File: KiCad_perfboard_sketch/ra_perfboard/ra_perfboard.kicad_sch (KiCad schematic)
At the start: 20 parts, among them J1 M1, J10 L6, J2 M2, J3 Terminal, J4 USART, J5 L3, J6 L1, J7 L2, J8 L4, J9 L5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

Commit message: Removed bug in LUT set speed function. Updates to MATLAB GUI and KiCad perfboard. Successfully tested TCA9548A library.
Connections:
- net M2_DIR: now also U4.7 (PA1); no longer U4.9 (PA3)
- net M2_EN: now also U4.9 (PA3); no longer U4.10 (PA4)
- net M2_STEP: now also U4.8 (PA2); no longer U4.11 (PA5)
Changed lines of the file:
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@@
 	(wire
 		(pts
-			(xy 130.81 66.04) (xy 129.54 66.04)
+			(xy 40.64 120.65) (xy 40.64 121.92)
+		)
+		(stroke
+			(width 0)
+			(type default)
+		)
+	)
+	(wire
+		(pts
+			(xy 158.75 74.93) (xy 160.02 74.93)
+		)
+		(stroke
+			(width 0)
+			(type default)
+		)
+	)
+	(wire
+		(pts
+			(xy 74.93 147.32) (xy 76.2 147.32)
+		)
+		(stroke
+			(width 0)
+			(type default)
+		)
+	)
+	(wire
+		(pts
+			(xy 158.75 44.45) (xy 157.48 44.45)
+		)
+		(stroke
+			(width 0)
+			(type default)
+		)
+	)
+	(wire
+		(pts
+			(xy 111.76 100.33) (xy 111.76 101.6)
+		)
+		(stroke
+			(width 0)
+			(type default)
+		)
+	)
+	(wire
+		(pts
+			(xy 55.88 121.92) (xy 54.61 121.92)
+		)
+		(stroke
+			(width 0)
+			(type default)
+		)
+	)
+	(wire
+		(pts
+			(xy 43.18 151.13) (xy 45.72 151.13)
+		)
+		(stroke
+			(width 0)
+			(type default)
+		)
+	)
+	(wire
+		(pts
+			(xy 130.81 60.96) (xy 129.54 60.96)
+		)
+		(stroke
+			(width 0)
+			(type default)
+		)
+	)
+	(wire
+		(pts
+			(xy 100.33 134.62) (xy 99.06 134.62)
+		)
+		(stroke
+			(width 0)
+			(type default)
+		)
+	)
+	(wire
+		(pts
+			(xy 167.64 100.33) (xy 162.56 100.33)
+		)
+		(stroke
+			(width 0)
+			(type default)
+		)
+	)
+	(wire
+		(pts
+			(xy 90.17 121.92) (xy 90.17 125.73)
+		)
+		(stroke
+			(width 0)
+			(type default)
+		)
+	)
+	(wire
+		(pts
+			(xy 109.22 100.33) (xy 111.76 100.33)
+		)
+		(stroke
+			(width 0)
+			(type default)
+		)
+	)
+	(wire
+		(pts
+			(xy 100.33 137.16) (xy 99.06 137.16)
+		)
+		(stroke
+			(width 0)
+			(type default)
+		)
+	)
+	(wire
+		(pts
+			(xy 85.09 121.92) (xy 85.09 125.73)
+		)
+		(stroke
+			(width 0)
+			(type default)
+		)
+	)
+	(wire
+		(pts
+			(xy 39.37 121.92) (xy 40.64 121.92)
+		)
+		(stroke
+			(width 0)
+			(type default)
+		)
+	)
+	(wire
+		(pts
+			(xy 130.81 78.74) (xy 129.54 78.74)
+		)
+		(stroke
+			(width 0)
+			(type default)
+		)
+	)
+	(wire
+		(pts
+			(xy 100.33 142.24) (xy 99.06 142.24)
+		)
+		(stroke
+			(width 0)
+			(type default)
+		)
+	)
+	(wire
+		(pts
+			(xy 85.09 120.65) (xy 85.09 121.92)
+		)
+		(stroke
+			(width 0)
+			(type default)
+		)
+	)
+	(wire
+		(pts
+			(xy 45.72 121.92) (xy 45.72 125.73)
+		)
+		(stroke
+			(width 0)
+			(type default)
+		)
+	)
+	(wire
+		(pts
+			(xy 90.17 120.65) (xy 90.17 121.92)
+		)
+		(stroke
+			(width 0)
+			(type default)
+		)
+	)
+	(wire
+		(pts
+			(xy 40.64 151.13) (xy 43.18 151.13)
+		)
+		(stroke
+			(width 0)
+			(type default)
+		)
+	)
+	(wire
+		(pts
+			(xy 100.33 139.7) (xy 99.06 139.7)
+		)
+		(stroke
+			(width 0)
+			(type default)
+		)
+	)
+	(wire
+		(pts
+			(xy 130.81 55.88) (xy 129.54 55.88)
+		)
+		(stroke
+			(width 0)
+			(type default)
+		)
+	)
+	(wire
+		(pts
+			(xy 92.71 52.07) (xy 93.98 52.07)
+		)
+		(stroke
+			(width 0)
+			(type default)
+		)
+	)
+	(wire
+		(pts
+			(xy 130.81 58.42) (xy 129.54 58.42)
 		)
 		(stroke
@@
 		(pts
 			(xy 130.81 63.5) (xy 129.54 63.5)
-		)
-		(stroke
-			(width 0)
-			(type default)
-		)
-	)
-	(wire
-		(pts
-			(xy 40.64 120.65) (xy 40.64 121.92)
-		)
-		(stroke
-			(width 0)
-			(type default)
-		)
-	)
-	(wire
-		(pts
-			(xy 158.75 74.93) (xy 160.02 74.93)
-		)
-		(stroke
-			(width 0)
-			(type default)
-		)
-	)
-	(wire
-		(pts
-			(xy 74.93 147.32) (xy 76.2 147.32)
-		)
-		(stroke
-			(width 0)
-			(type default)
-		)
-	)
-	(wire
-		(pts
-			(xy 158.75 44.45) (xy 157.48 44.45)
-		)
-		(stroke
-			(width 0)
-			(type default)
-		)
-	)
-	(wire
-		(pts
-			(xy 111.76 100.33) (xy 111.76 101.6)
-		)
-		(stroke
-			(width 0)
-			(type default)
-		)
-	)
-	(wire
-		(pts
-			(xy 55.88 121.92) (xy 54.61 121.92)
-		)
-		(stroke
-			(width 0)
-			(type default)
-		)
-	)
-	(wire
-		(pts
-			(xy 43.18 151.13) (xy 45.72 151.13)
-		)
-		(stroke
-			(width 0)
-			(type default)
-		)
-	)
-	(wire
-		(pts
-			(xy 100.33 134.62) (xy 99.06 134.62)
-		)
-		(stroke
-			(width 0)
-			(type default)
-		)
-	)
-	(wire
-		(pts
-			(xy 167.64 100.33) (xy 162.56 100.33)
-		)
-		(stroke
-			(width 0)
-			(type default)
-		)
-	)
-	(wire
-		(pts
-			(xy 90.17 121.92) (xy 90.17 125.73)
-		)
-		(stroke
-			(width 0)
-			(type default)
-		)
-	)
-	(wire
-		(pts
-			(xy 109.22 100.33) (xy 111.76 100.33)
-		)
-		(stroke
-			(width 0)
-			(type default)
-		)
-	)
-	(wire
-		(pts
-			(xy 100.33 137.16) (xy 99.06 137.16)
-		)
-		(stroke
-			(width 0)
-			(type default)
-		)
-	)
-	(wire
-		(pts
-			(xy 85.09 121.92) (xy 85.09 125.73)
-		)
-		(stroke
-			(width 0)
-			(type default)
-		)
-	)
-	(wire
-		(pts
-			(xy 39.37 121.92) (xy 40.64 121.92)
-		)
-		(stroke
-			(width 0)
-			(type default)
-		)
-	)
-	(wire
-		(pts
-			(xy 130.81 78.74) (xy 129.54 78.74)
-		)
-		(stroke
-			(width 0)
-			(type default)
-		)
-	)
-	(wire
-		(pts
-			(xy 100.33 142.24) (xy 99.06 142.24)
-		)
-		(stroke
-			(width 0)
-			(type default)
-		)
-	)
-	(wire
-		(pts
-			(xy 85.09 120.65) (xy 85.09 121.92)
-		)
-		(stroke
-			(width 0)
-			(type default)
-		)
-	)
-	(wire
-		(pts
-			(xy 45.72 121.92) (xy 45.72 125.73)
-		)
-		(stroke
-			(width 0)
-			(type default)
-		)
-	)
-	(wire
-		(pts
-			(xy 90.17 120.65) (xy 90.17 121.92)
-		)
-		(stroke
-			(width 0)
-			(type default)
-		)
-	)
-	(wire
-		(pts
-			(xy 40.64 151.13) (xy 43.18 151.13)
-		)
-		(stroke
-			(width 0)
-			(type default)
-		)
-	)
-	(wire
-		(pts
-			(xy 100.33 139.7) (xy 99.06 139.7)
-		)
-		(stroke
-			(width 0)
-			(type default)
-		)
-	)
-	(wire
-		(pts
-			(xy 130.81 55.88) (xy 129.54 55.88)
-		)
-		(stroke
-			(width 0)
-			(type default)
-		)
-	)
-	(wire
-		(pts
-			(xy 92.71 52.07) (xy 93.98 52.07)
-		)
-		(stroke
-			(width 0)
-			(type default)
-		)
-	)
-	(wire
-		(pts
-			(xy 130.81 68.58) (xy 129.54 68.58)
 		)
 		(stroke
@@
 	)
 	(label "M2_STEP"
-		(at 130.81 68.58 0)
+		(at 130.81 60.96 0)
 		(effects
 			(font
@@
 	)
 	(label "M2_DIR"
-		(at 130.81 63.5 0)
+		(at 130.81 58.42 0)
 		(effects
 			(font
@@
 	)
 	(label "M2_EN"
-		(at 130.81 66.04 0)
-		(effects
-			(font
+		(at 130.81 63.5 0)
+		(effects
+			(font

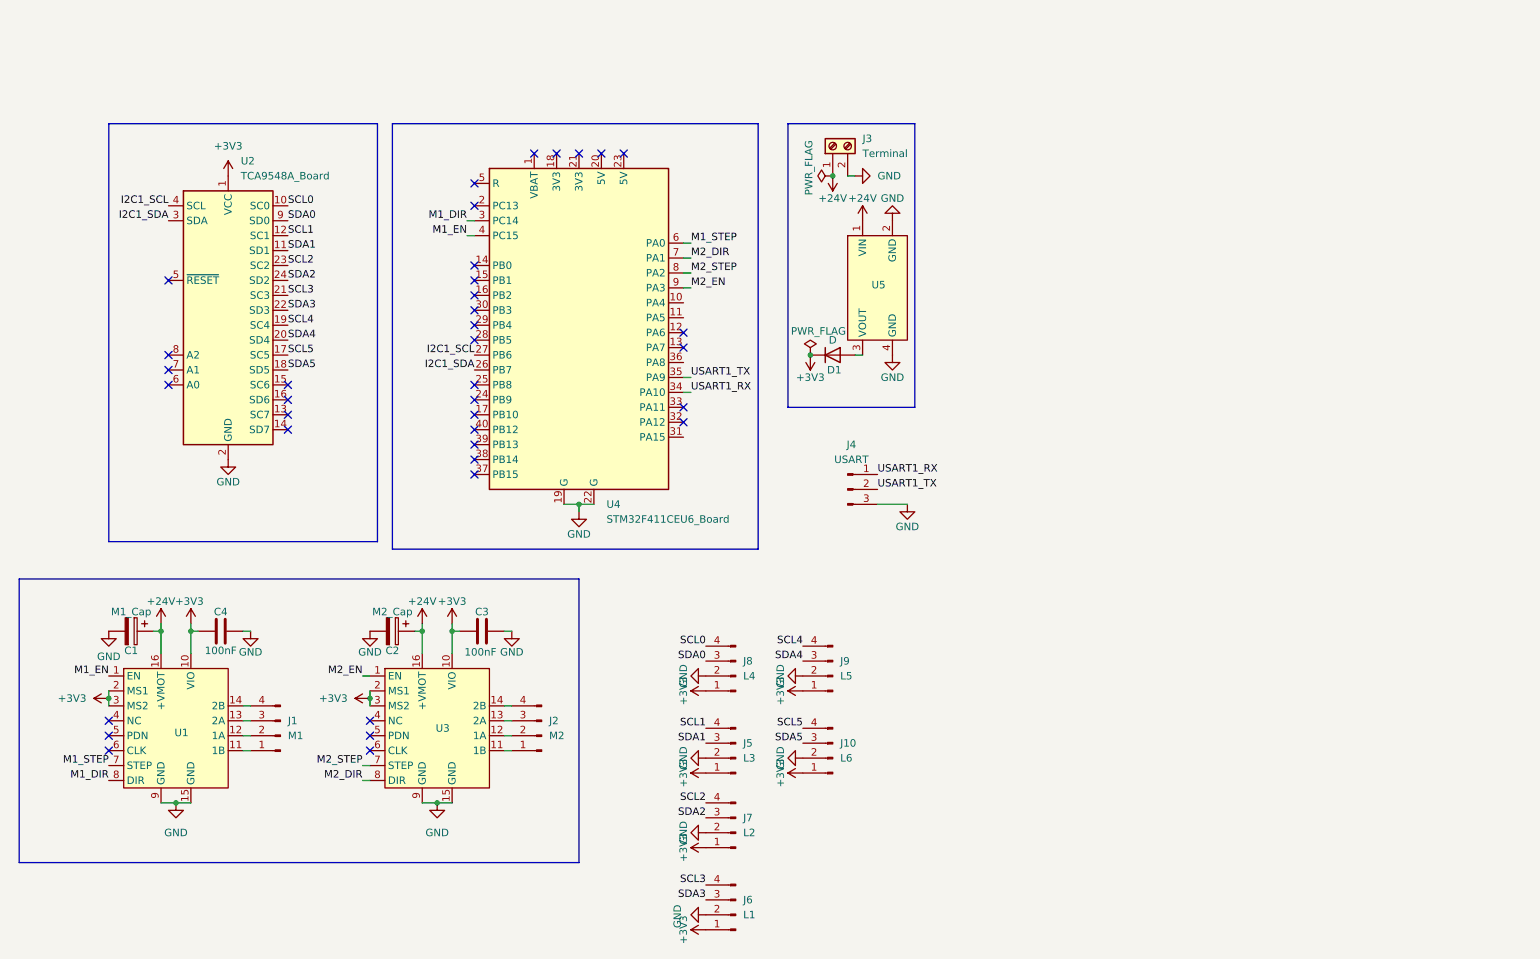
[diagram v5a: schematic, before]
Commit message: Modified AS5600_Mux library and added DMA functionality.
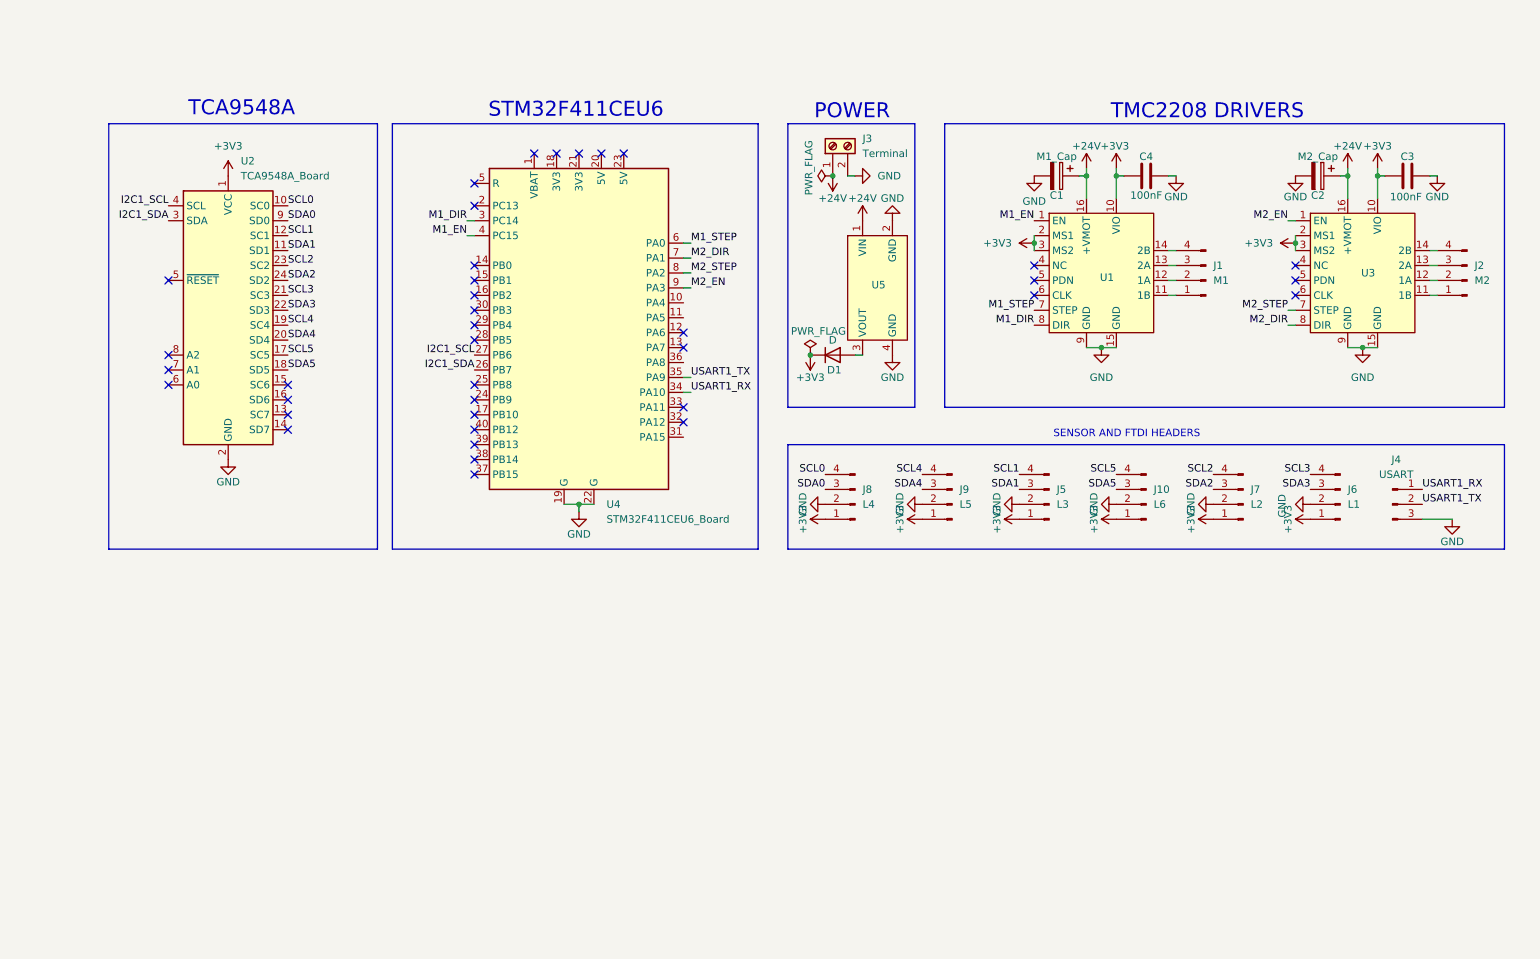
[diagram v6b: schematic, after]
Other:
- note added: "POWER"
- note added: "SENSOR AND FTDI HEADERS"
- note added: "STM32F411CEU6"
- note added: "TCA9548A"
- note added: "TMC2208 DRIVERS"
- moved on the sheet: C1, C2, C3, C4, J1, J10, J2, J4, J5, J6, J7, J8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
